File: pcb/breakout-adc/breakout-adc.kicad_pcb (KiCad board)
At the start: 4 copper layers, 100 x 62 mm, 104 parts, among them J1 Screw_Terminal_01x04, J10 Conn_01x01_Pin, J11 Conn_01x12_Pin, J12 Conn_01x12_Pin, J13 Conn_01x01_Pin, J14 Conn_01x01_Pin, J15 FX18-120P-0.8SV20, J2 Screw_Terminal_01x02, J20 Conn_02x02_Counter_Clockwise, J21 Conn_02x04_Odd_Even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

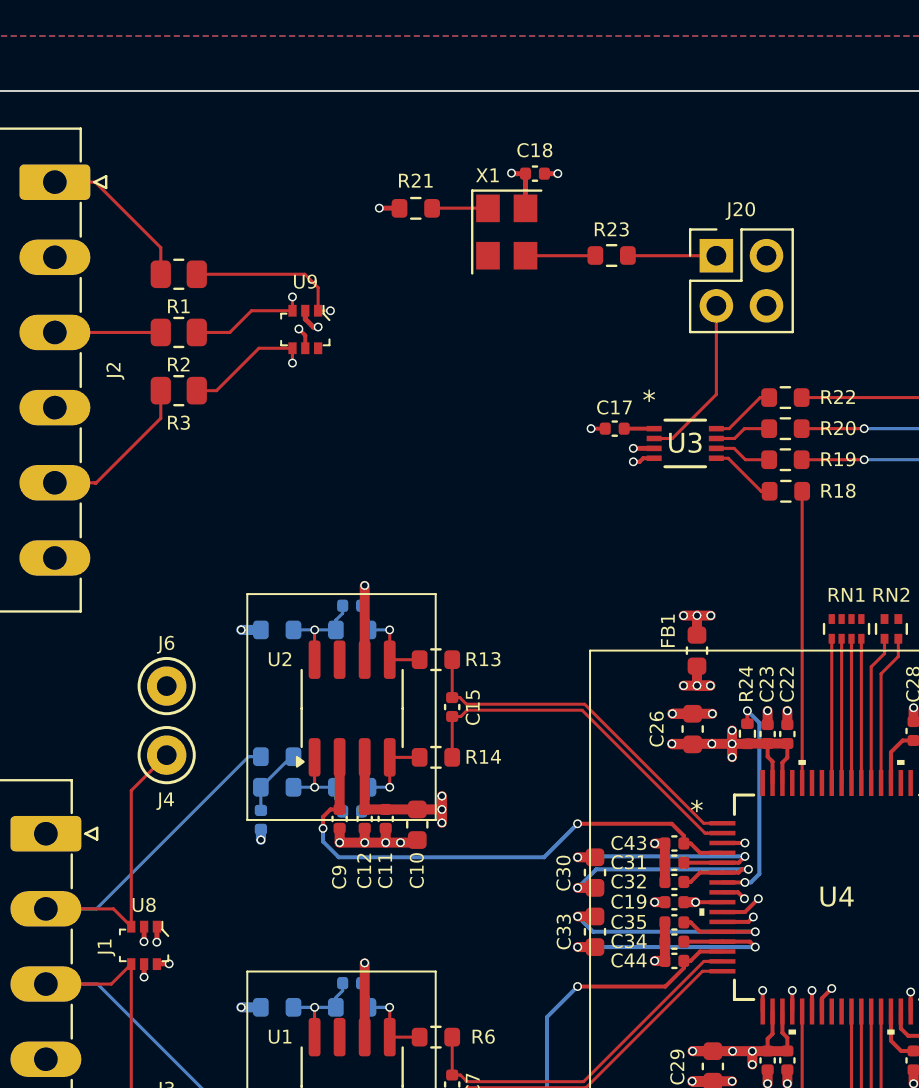
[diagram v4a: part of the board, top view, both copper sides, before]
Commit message: [adc][pcb] set 3dmodels
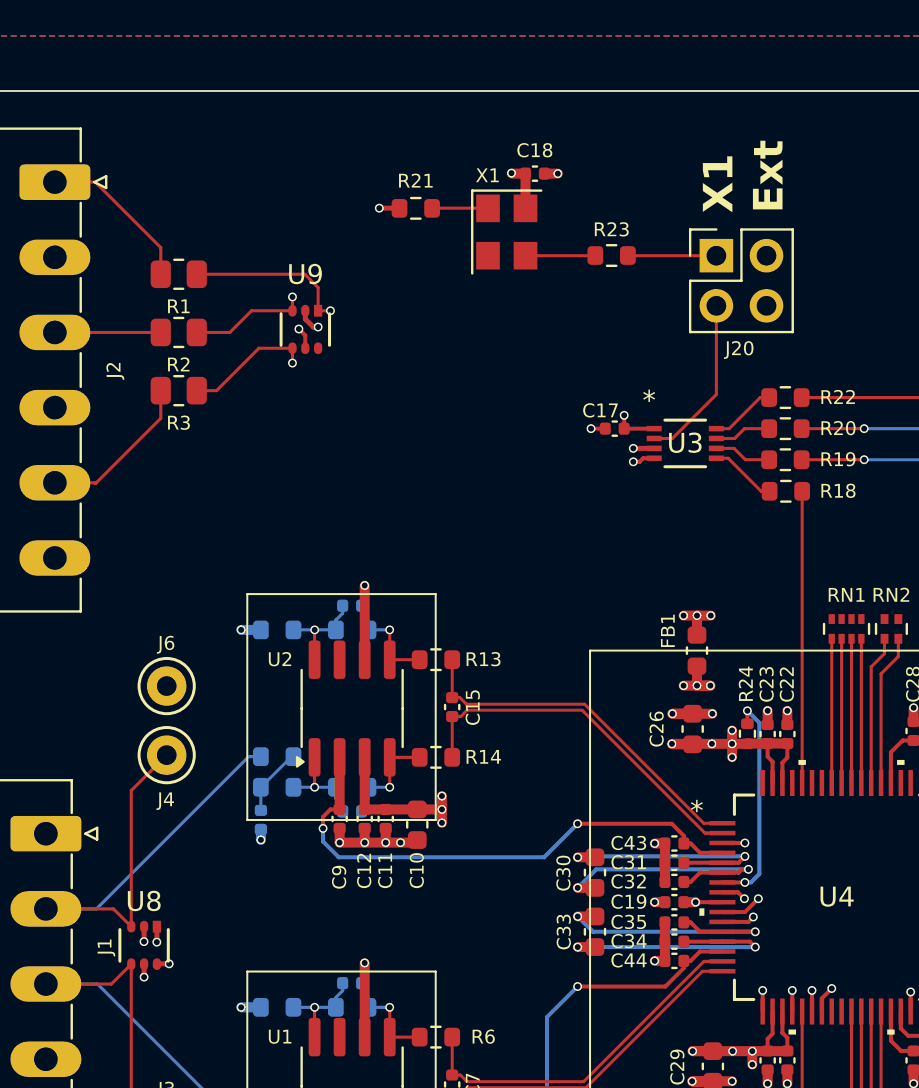
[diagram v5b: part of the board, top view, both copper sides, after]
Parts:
- U8, U9: footprint digikey-footprints:SOT-363 -> D1213A:SOT-363_DIO
- turned U8 to -90 degrees
- turned U9 to -90 degrees
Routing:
- net +3V3: track 33.1 -> 33.8 mm, vias 8 -> 9
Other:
- board text added: "Ext"
- board text added: "X1"

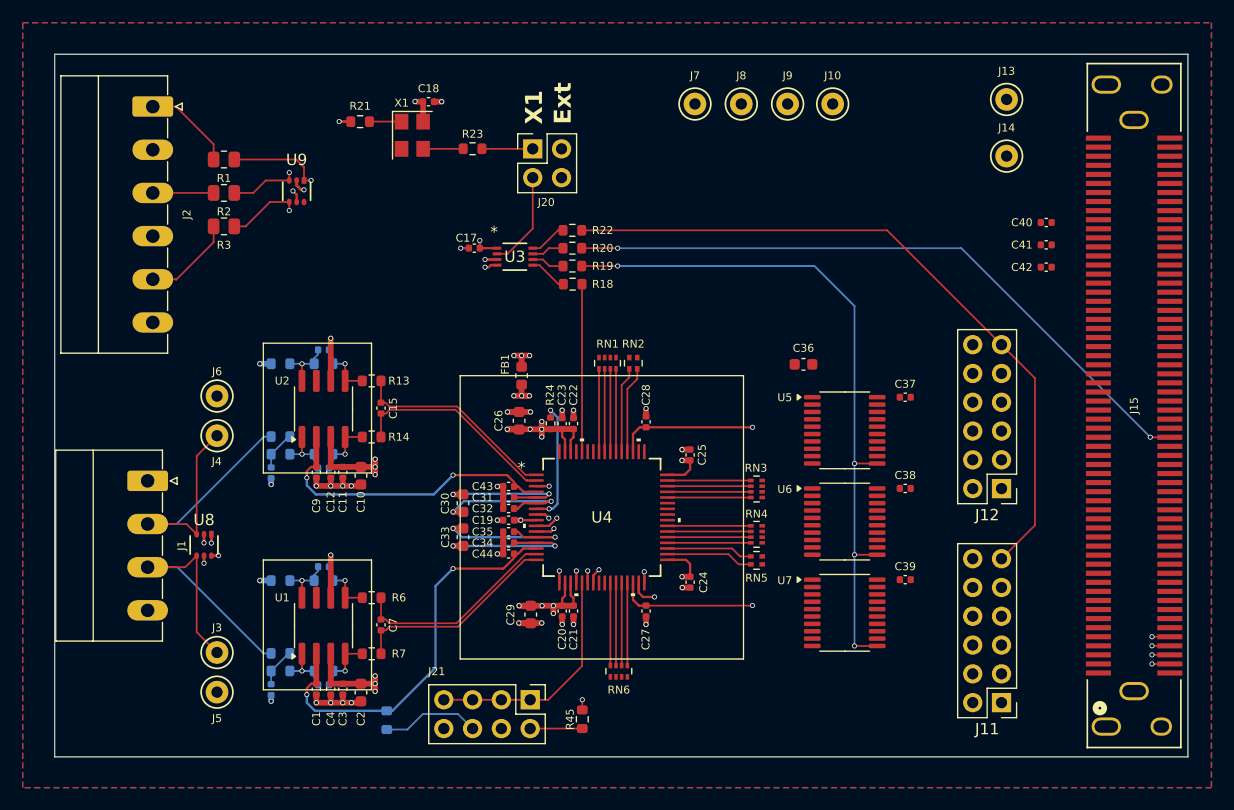
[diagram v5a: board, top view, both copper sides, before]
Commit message: [adc][pcb] adc jumper select silks
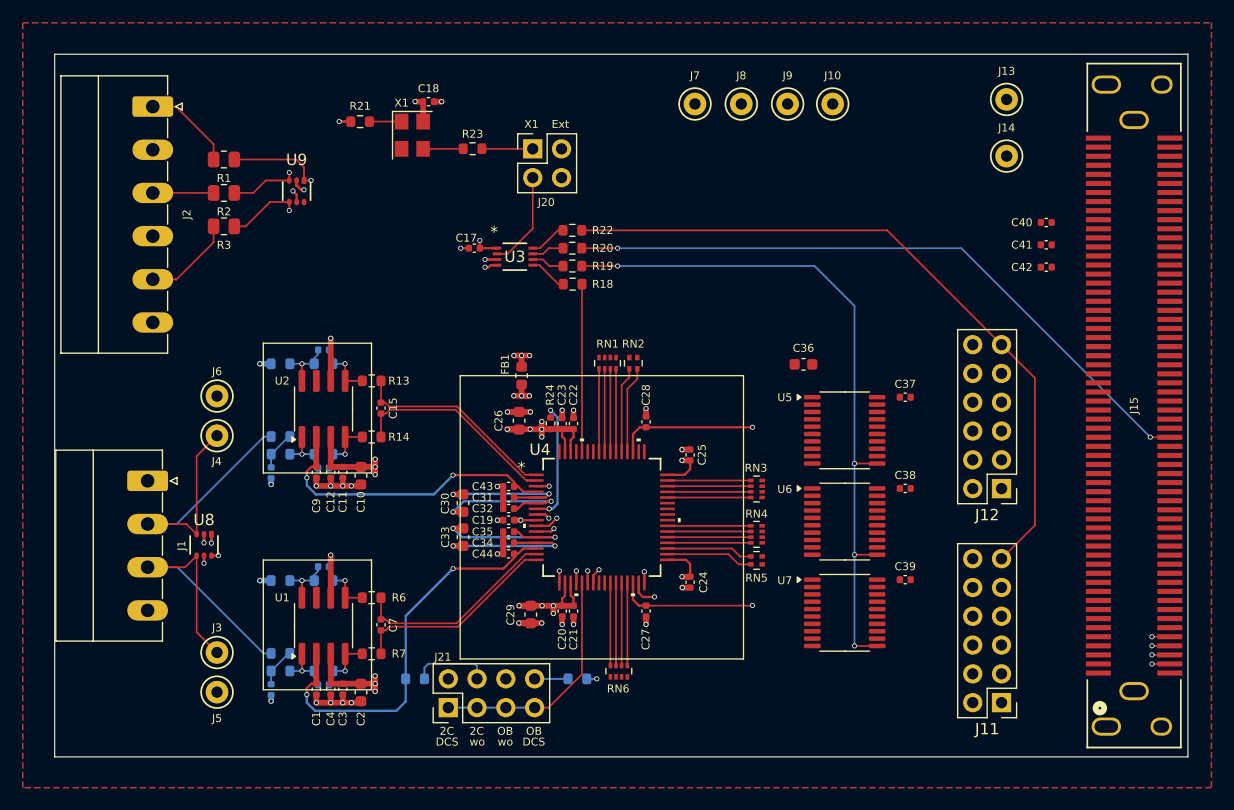
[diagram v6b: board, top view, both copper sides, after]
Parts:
- R45: moved to B.Cu
- moved J21 7.26 mm to (143.4, 101.2), turned to 90 degrees
- moved R46 4.42 mm to (140.5, 98.7), turned to 0 degrees
- moved R45 3.59 mm to (154.8, 98.7), turned to 180 degrees
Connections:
- J21 pad 2: Net-(J21-Pin_2) -> GND
- J21 pad 4: unconnected-(J21-Pin_4-Pad4) -> Net-(J21-Pin_4)
- J21 pad 6: Net-(J21-Pin_6) -> unconnected-(J21-Pin_6-Pad6)
- J21 pad 8: GND -> Net-(J21-Pin_8)
- R45 pad 2: Net-(J21-Pin_2) -> Net-(J21-Pin_8)
- R46 pad 2: Net-(J21-Pin_6) -> Net-(J21-Pin_4)
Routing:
- net Net-(J21-Pin_6): track 8.68 -> 0.00 mm
- net Net-(J21-Pin_4): track 0.00 -> 6.98 mm
- net Net-(J21-Pin_2): track 4.60 -> 0.00 mm
- net Net-(J21-Pin_8): track 0.00 -> 2.95 mm
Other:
- board text added: "2C"
- board text added: "DCS"
- board text added: "OB"
- board text added: "wo"

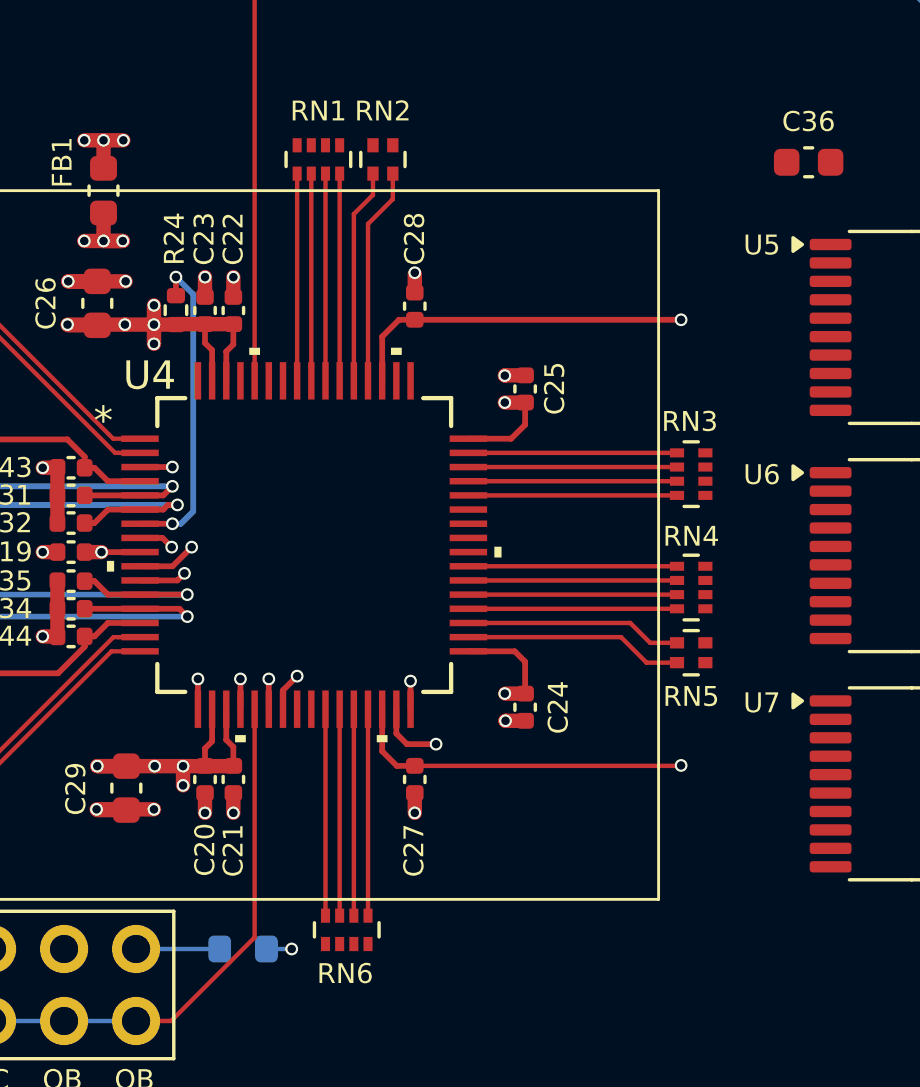
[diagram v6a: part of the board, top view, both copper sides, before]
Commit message: [adc][pcb] adc gnd routing (special DRGND handling)
Note the potentially weird/wrong DRGND routing documented
in layout.md
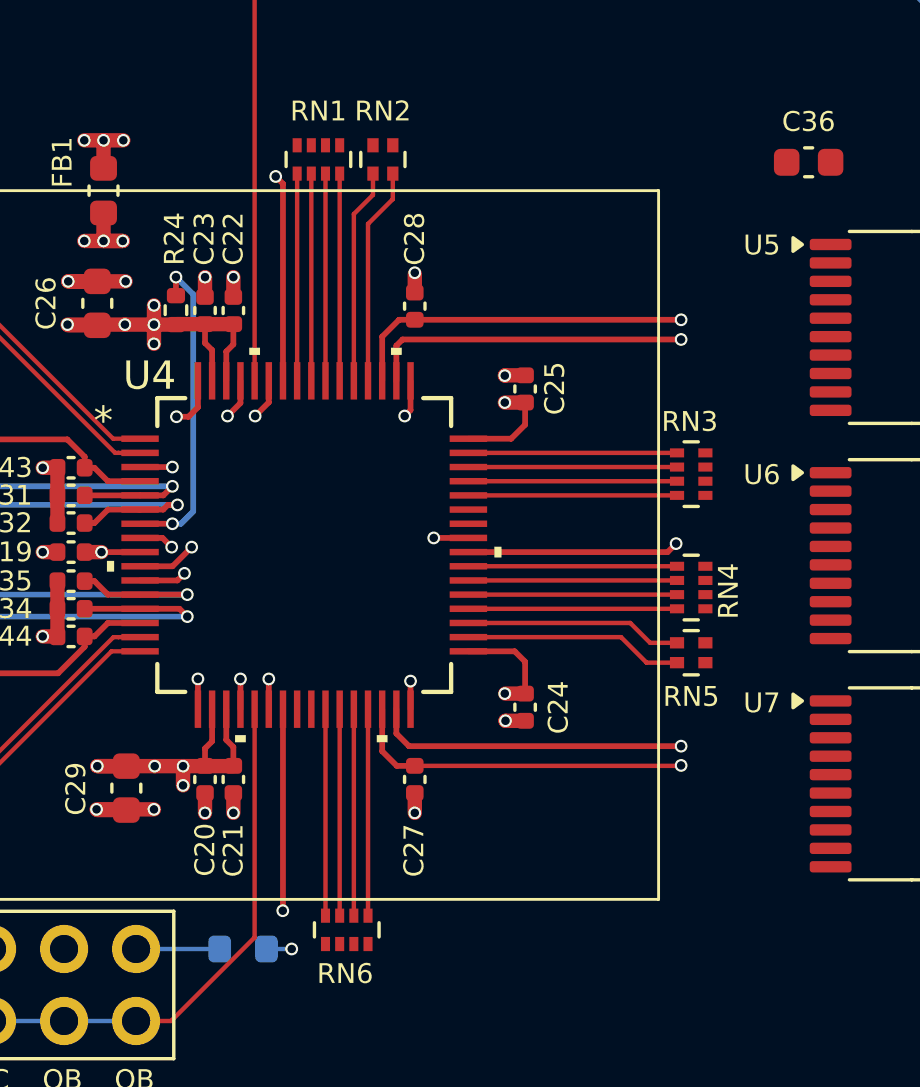
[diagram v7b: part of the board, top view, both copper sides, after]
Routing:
- net GND: track 62.7 -> 110.5 mm, vias 48 -> 56
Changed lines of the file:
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@@
 		(tags "resistor array")
 		(property "Reference" "RN4"
-			(at 0 -1.8 0)
+			(at 1.318334 0.124999 90)
 			(unlocked yes)
 			(layer "F.SilkS")
@@
 	)
 	(segment
-		(start 156.206665 89.525001)
-		(end 156.706666 89.025)
-		(width 0.2032)
-		(layer "F.Cu")
-		(net 1)
-	)
-	(segment
 		(start 133.035 80.91)
 		(end 133.035 81.63)
@@
 	)
 	(segment
+		(start 160.706666 78.6088)
+		(end 160.706666 79.643334)
+		(width 0.2032)
+		(layer "F.Cu")
+		(net 1)
+	)
+	(segment
+		(start 160.651863 91.495197)
+		(end 160.206667 91.050001)
+		(width 0.2032)
+		(layer "F.Cu")
+		(net 1)
+	)
+	(segment
 		(start 122.504509 85.89)
 		(end 122.504509 86.670491)
@@
 	)
 	(segment
+		(start 156.206665 90.1912)
+		(end 156.206665 97.293335)
+		(width 0.2032)
+		(layer "F.Cu")
+		(net 1)
+	)
+	(segment
 		(start 134.1 100.04)
 		(end 134.1 100.76)
@@
 	)
 	(segment
+		(start 153.206666 78.6088)
+		(end 153.206666 79.543334)
+		(width 0.2032)
+		(layer "F.Cu")
+		(net 1)
+	)
+	(segment
+		(start 153.206666 79.543334)
+		(end 152.875 79.875)
+		(width 0.2032)
+		(layer "F.Cu")
+		(net 1)
+	)
+	(segment
 		(start 148.251666 81.675)
 		(end 147.731666 81.675)
@@
 	)
 	(segment
+		(start 155.225 79.85)
+		(end 155.706666 79.368334)
+		(width 0.2032)
+		(layer "F.Cu")
+		(net 1)
+	)
+	(segment
+		(start 154.25 79.85)
+		(end 154.706665 79.393335)
+		(width 0.2032)
+		(layer "F.Cu")
+		(net 1)
+	)
+	(segment
 		(start 133.035 91.489666)
 		(end 133.035 87.745)
@@
 	)
 	(segment
-		(start 156.206665 90.1912)
-		(end 156.206665 89.525001)
+		(start 152.481666 85.65)
+		(end 151.165466 85.65)
 		(width 0.2032)
 		(layer "F.Cu")
@@
 	)
 	(segment
-		(start 152.481666 85.65)
-		(end 151.165466 85.65)
+		(start 170.25 91.495197)
+		(end 160.651863 91.495197)
 		(width 0.2032)
 		(layer "F.Cu")
@@
 	)
 	(segment
-		(start 161.606666 91.425)
-		(end 160.581666 91.425)
-		(width 0.2032)
-		(layer "F.Cu")
-		(net 1)
-	)
-	(segment
 		(start 121.854509 85.890001)
 		(end 121.854509 86.645491)
@@
 	)
 	(segment
-		(start 152.986469 84.475)
-		(end 152.311468 85.150001)
+		(start 160.206667 78.6088)
+		(end 160.206667 77.368333)
 		(width 0.2032)
 		(layer "F.Cu")
@@
 	)
 	(segment
-		(start 121.854509 86.645491)
-		(end 121.85 86.65)
-		(width 0.254)
+		(start 162.747866 84.15)
+		(end 161.525 84.15)
+		(width 0.2032)
 		(layer "F.Cu")
 		(net 1)
 	)
 	(segment
-		(start 160.581666 91.425)
-		(end 160.206667 91.050001)
+		(start 152.986469 84.475)
+		(end 152.311468 85.150001)
 		(width 0.2032)
 		(layer "F.Cu")
@@
 	)
 	(segment
+		(start 121.854509 86.645491)
+		(end 121.85 86.65)
+		(width 0.254)
+		(layer "F.Cu")
+		(net 1)
+	)
+	(segment
 		(start 149.656666 93.75)
 		(end 150.681666 93.75)
@@
 	)
 	(segment
+		(start 155.706666 79.368334)
+		(end 155.706666 78.6088)
+		(width 0.2032)
+		(layer "F.Cu")
+		(net 1)
+	)
+	(segment
+		(start 160.206667 77.368333)
+		(end 160.425 77.15)
+		(width 0.2032)
+		(layer "F.Cu")
+		(net 1)
+	)
+	(segment
 		(start 131.765 100.04)
 		(end 131.765 100.76)
@@
 	)
 	(segment
-		(start 160.206667 91.050001)
-		(end 160.206667 90.1912)
+		(start 160.425 77.15)
+		(end 170.25 77.15)
 		(width 0.2032)
 		(layer "F.Cu")
@@
 	)
 	(segment
+		(start 156.206665 97.293335)
+		(end 156.2 97.3)
+		(width 0.2032)
+		(layer "F.Cu")
+		(net 1)
+	)
+	(segment
 		(start 135.57 100.76)
 		(end 135.7 100.63)
@@
 	)
 	(segment
+		(start 170.075 84.35)
+		(end 169.775 84.65)
+		(width 0.2032)
+		(layer "F.Cu")
+		(net 1)
+	)
+	(segment
+		(start 160.206667 91.050001)
+		(end 160.206667 90.1912)
+		(width 0.2032)
+		(layer "F.Cu")
+		(net 1)
+	)
+	(segment
 		(start 147.706866 61.65)
 		(end 146.65 61.65)
@@
 	)
 	(segment
+		(start 152.875 79.875)
+		(end 152.45 79.875)
+		(width 0.2032)
+		(layer "F.Cu")
+		(net 1)
+	)
+	(segment
+		(start 169.775 84.65)
+		(end 162.747866 84.65)
+		(width 0.2032)
+		(layer "F.Cu")
+		(net 1)
+	)
+	(segment
 		(start 149.631666 93.725)
 		(end 151.656666 93.725)
@@
 	)
 	(segment
+		(start 154.706665 79.393335)
+		(end 154.706665 78.6088)
+		(width 0.2032)
+		(layer "F.Cu")
+		(net 1)
+	)
+	(segment
+		(start 156.206665 78.6088)
+		(end 156.206665 71.656665)
+		(width 0.2032)
+		(layer "F.Cu")
+		(net 1)
+	)
+	(segment
 		(start 154.456667 93.15)
 		(end 154.456667 93.849999)
@@
 	)
 	(segment
+		(start 156.206665 71.656665)
+		(end 155.95 71.4)
+		(width 0.2032)
+		(layer "F.Cu")
+		(net 1)
+	)
+	(segment
 		(start 133.035 100.04)
 		(end 133.035 100.76)
@@
 		(net 1)
 	)
+	(segment
+		(start 160.706666 79.643334)
+		(end 160.5 79.85)
+		(width 0.2032)
+		(layer "F.Cu")
+		(net 1)
+	)
 	(via
 		(at 131.765 100.76)
@@
 	)
 	(via
+		(at 155.95 71.4)
+		(size 0.45)
+		(drill 0.3)
+		(layers "F.Cu" "B.Cu")
+		(net 1)
+	)
+	(via
 		(at 144.506666 60.65)
 		(size 0.45)
@@
 	)
 	(via
+		(at 154.25 79.85)
+		(size 0.45)
+		(drill 0.3)
+		(layers "F.Cu" "B.Cu")
+		(net 1)
+	)
+	(via
 		(at 133.035 68.6)
 		(size 0.45)
@@
 	)
 	(via
-		(at 161.606666 91.425)
+		(at 170.075 84.35)
+		(size 0.45)
+		(drill 0.3)
+		(layers "F.Cu" "B.Cu")
+		(net 1)
+	)
+	(via
+		(at 170.25 77.15)
+		(size 0.45)
+		(drill 0.3)
+		(layers "F.Cu" "B.Cu")
+		(net 1)
+	)
+	(via
+		(at 170.25 91.495197)
+		(size 0.45)
+		(drill 0.3)
+		(layers "F.Cu" "B.Cu")
+		(net 1)
+	)
+	(via
+		(at 156.2 97.3)
 		(size 0.45)
 		(drill 0.3)
@@
 	)
 	(via
-		(at 156.706666 89.025)
-		(size 0.45)
-		(drill 0.3)
-		(layers "F.Cu" "B.Cu")
-		(net 1)
-	)
-	(via
 		(at 152.731666 85.4)
 		(size 0.45)
@@
 	)
 	(via
+		(at 161.525 84.15)
+		(size 0.45)
+		(drill 0.3)
+		(layers "F.Cu" "B.Cu")
+		(net 1)
+	)
+	(via
+		(at 152.45 79.875)
+		(size 0.45)
+		(drill 0.3)
+		(layers "F.Cu" "B.Cu")
+		(net 1)
+	)
+	(via
 		(at 155.706666 89.125)
 		(size 0.45)
@@
 	)
 	(via
+		(at 160.5 79.85)
+		(size 0.45)
+		(drill 0.3)
+		(layers "F.Cu" "B.Cu")
+		(net 1)
+	)
+	(via
 		(at 130.675 55.5)
 		(size 0.45)
 		(drill 0.3)
+		(layers "F.Cu" "B.Cu")
+		(net 1)
+	)
+	(via
+		(at 155.225 79.85)
+		(size 0.45)
+		(drill 0.3)
